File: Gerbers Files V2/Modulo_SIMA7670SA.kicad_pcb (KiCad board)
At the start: 2 copper layers, 92 x 85 mm, 62 parts, among them J1 TBP01R1-508-02BE, J2 DB9 Hembra Impreso 90°, J3 U.FL IPEX1 MALE, J4 SMA-J-P-X-RA-TH1, J5 Jack DC 2.1mm PCB recto, Q1 BSS138, Q2 FDN340P, Q3 FDN340P, Q4 BSS138, U1 MAX3232E, U2 24LC512, U3 BKP-A7670SA (Módulo SIMCOM), U5 Black_Pill_STM32F411CEUx, U6 LM2596S_Modulo_Regulable, U7 LM7805_TO220

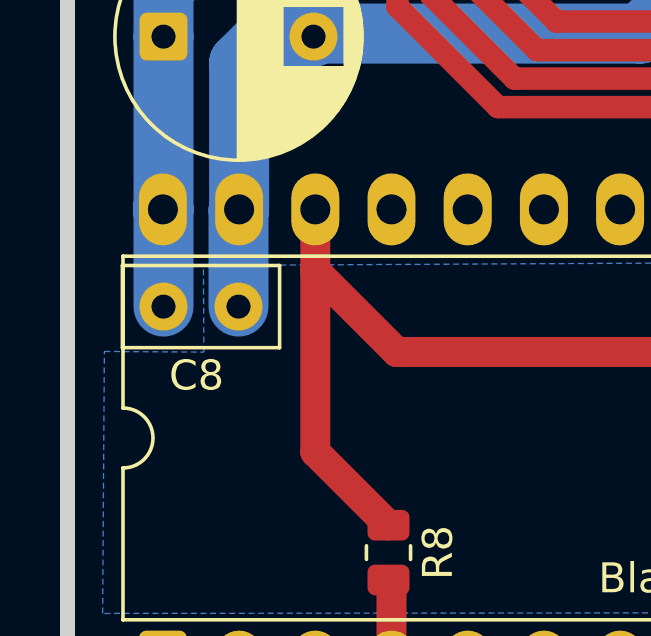
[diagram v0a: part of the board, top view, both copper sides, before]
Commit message: Layout PCB finalizado + archivos de fabricación
- Ruteo completo del PCB (2 capas, FR4 1.6mm/1oz, ~92x85mm, 62 componentes, KiCad 10)
- Dominio de alimentación del modem independiente en cobre (12V_StepDown/5V_MODEM separados de 3V3): brownout resuelto
- RS232 pasado del esquema al layout; planos GND F.Cu/B.Cu + zona +12V
- Generados Gerbers y drill Excellon para fabricación.
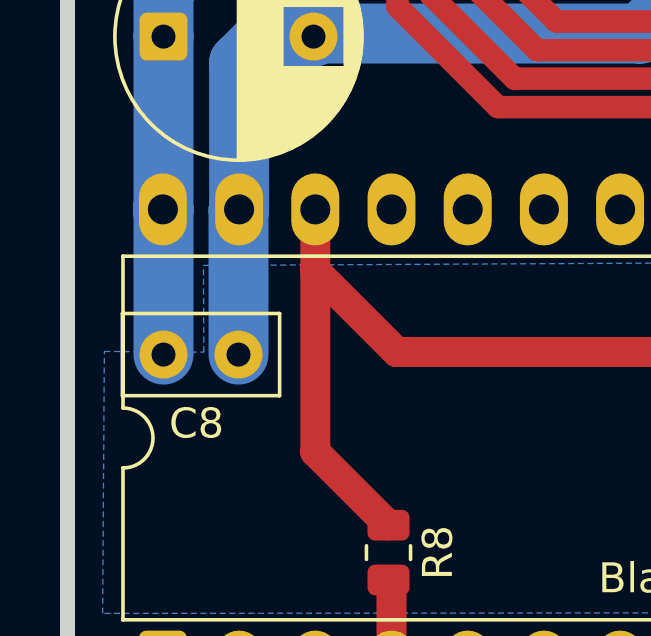
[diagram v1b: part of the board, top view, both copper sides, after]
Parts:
- moved C8 1.60 mm to (118.1, 102.1)
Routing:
- net GND: track 355.6 -> 357.2 mm
- net +5V: track 50.0 -> 51.6 mm
